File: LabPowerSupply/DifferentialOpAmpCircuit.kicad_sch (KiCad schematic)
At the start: 11 parts

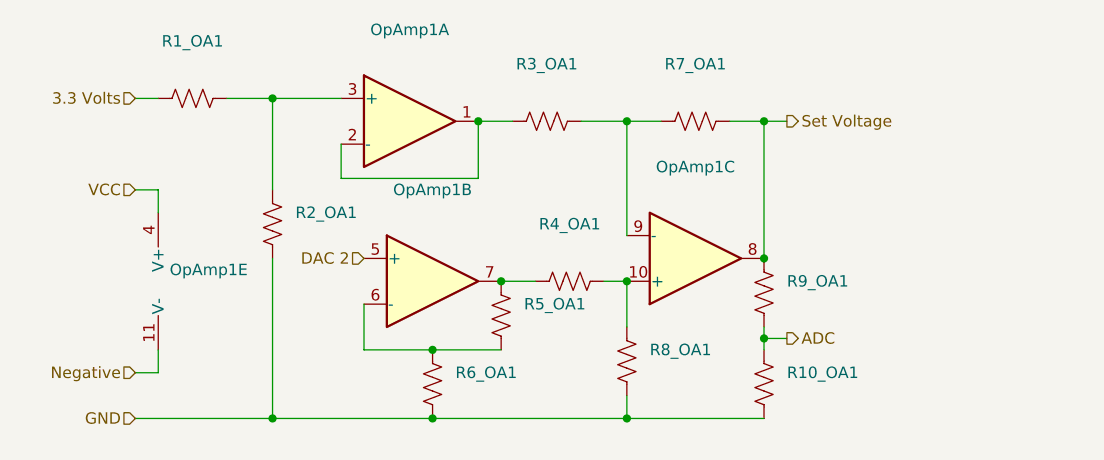
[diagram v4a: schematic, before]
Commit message: Added mcu capacitors, split 5v inductors
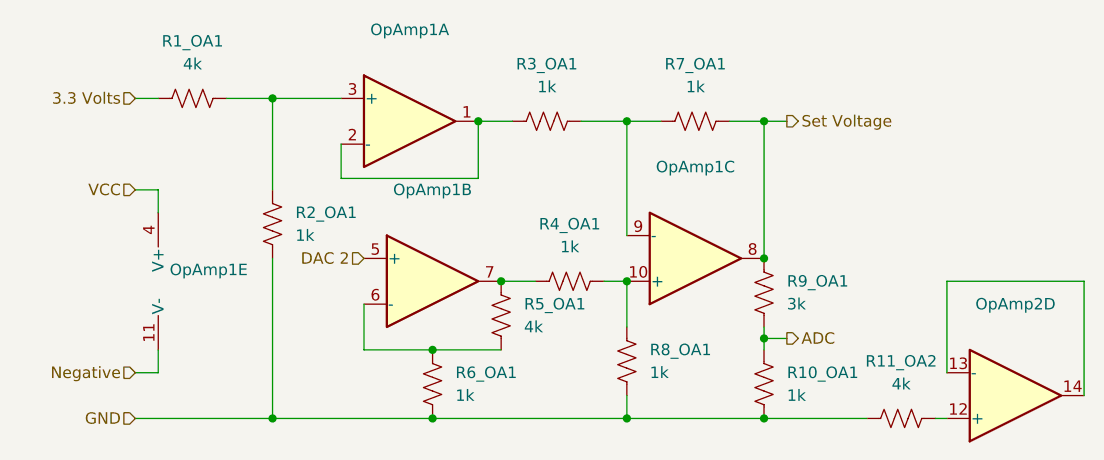
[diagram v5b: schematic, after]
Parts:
- added OpAmp2: (no value), symbol Amplifier_Operational:LM324
- added R11_OA2: 4k, Resistor_SMD:R_0603_1608Metric, symbol Device:R_US
- R10_OA1, R2_OA1, R3_OA1, R4_OA1, R6_OA1, R7_OA1, R8_OA1: value (none) -> 1k; footprint (none) -> Resistor_SMD:R_0603_1608Metric
- R1_OA1, R5_OA1: value (none) -> 4k; footprint (none) -> Resistor_SMD:R_0603_1608Metric
- R9_OA1: value (none) -> 3k; footprint (none) -> Resistor_SMD:R_0603_1608Metric
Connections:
- net GND: now also R11_OA2.1
- new net: OpAmp2.12 (+), R11_OA2.2
- new net: OpAmp2.13 (-), OpAmp2.14
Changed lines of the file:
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@@
   (junction (at 151.13 119.38) (diameter 0) (color 0 0 0 0)
   )
+  (junction (at 166.37 119.38) (diameter 0) (color 0 0 0 0)
+  )
   (junction (at 151.13 86.36) (diameter 0) (color 0 0 0 0)
   )
@@
     (stroke (width 0) (type default) (color 0 0 0 0))
   )
+  (wire (pts (xy 166.37 119.38) (xy 177.8 119.38))
+    (stroke (width 0) (type default) (color 0 0 0 0))
+  )
   (wire (pts (xy 148.59 104.14) (xy 151.13 104.14))
     (stroke (width 0) (type default) (color 0 0 0 0))
   )
+  (wire (pts (xy 201.93 104.14) (xy 186.69 104.14))
+    (stroke (width 0) (type default) (color 0 0 0 0))
+  )
   (wire (pts (xy 166.37 86.36) (xy 168.91 86.36))
     (stroke (width 0) (type default) (color 0 0 0 0))
@@
     (stroke (width 0) (type default) (color 0 0 0 0))
   )
+  (wire (pts (xy 201.93 116.84) (xy 201.93 104.14))
+    (stroke (width 0) (type default) (color 0 0 0 0))
+  )
+  (wire (pts (xy 185.42 119.38) (xy 186.69 119.38))
+    (stroke (width 0) (type default) (color 0 0 0 0))
+  )
   (wire (pts (xy 106.68 83.82) (xy 111.76 83.82))
     (stroke (width 0) (type default) (color 0 0 0 0))
   )
   (wire (pts (xy 140.97 104.14) (xy 137.16 104.14))
+    (stroke (width 0) (type default) (color 0 0 0 0))
+  )
+  (wire (pts (xy 186.69 104.14) (xy 186.69 114.3))
     (stroke (width 0) (type default) (color 0 0 0 0))
   )
@@
       (effects (font (size 1.27 1.27)) (justify left))
     )
-    (property "Value" "" (id 1) (at 168.91 106.6799 0)
-      (effects (font (size 1.27 1.27)) (justify left))
-    )
-    (property "Footprint" "" (id 2) (at 167.386 105.664 90)
+    (property "Value" "3k" (id 1) (at 168.91 106.6799 0)
+      (effects (font (size 1.27 1.27)) (justify left))
+    )
+    (property "Footprint" "Resistor_SMD:R_0603_1608Metric" (id 2) (at 167.386 105.664 90)
       (effects (font (size 1.27 1.27)) hide)
     )
@@
     (in_bom yes) (on_board yes) (fields_autoplaced)
     (property "Reference" "R3_OA1" (id 0) (at 142.24 80.01 90))
-    (property "Value" "" (id 1) (at 142.24 82.55 90))
-    (property "Footprint" "" (id 2) (at 142.494 85.344 90)
+    (property "Value" "1k" (id 1) (at 142.24 82.55 90))
+    (property "Footprint" "Resistor_SMD:R_0603_1608Metric" (id 2) (at 142.494 85.344 90)
       (effects (font (size 1.27 1.27)) hide)
     )
@@
     (in_bom yes) (on_board yes) (fields_autoplaced)
     (property "Reference" "R1_OA1" (id 0) (at 102.87 77.47 90))
-    (property "Value" "" (id 1) (at 102.87 80.01 90))
-    (property "Footprint" "" (id 2) (at 103.124 82.804 90)
+    (property "Value" "4k" (id 1) (at 102.87 80.01 90))
+    (property "Footprint" "Resistor_SMD:R_0603_1608Metric" (id 2) (at 103.124 82.804 90)
       (effects (font (size 1.27 1.27)) hide)
     )
@@
       (effects (font (size 1.27 1.27)) (justify left))
     )
-    (property "Value" "" (id 1) (at 114.3 99.0599 0)
-      (effects (font (size 1.27 1.27)) (justify left))
-    )
-    (property "Footprint" "" (id 2) (at 112.776 98.044 90)
+    (property "Value" "1k" (id 1) (at 114.3 99.0599 0)
+      (effects (font (size 1.27 1.27)) (justify left))
+    )
+    (property "Footprint" "Resistor_SMD:R_0603_1608Metric" (id 2) (at 112.776 98.044 90)
       (effects (font (size 1.27 1.27)) hide)
     )
@@
       (effects (font (size 1.27 1.27)) (justify left))
     )
-    (property "Value" "" (id 1) (at 132.08 116.8399 0)
-      (effects (font (size 1.27 1.27)) (justify left))
-    )
-    (property "Footprint" "" (id 2) (at 130.556 115.824 90)
+    (property "Value" "1k" (id 1) (at 132.08 116.8399 0)
+      (effects (font (size 1.27 1.27)) (justify left))
+    )
+    (property "Footprint" "Resistor_SMD:R_0603_1608Metric" (id 2) (at 130.556 115.824 90)
       (effects (font (size 1.27 1.27)) hide)
     )
@@
     (in_bom yes) (on_board yes) (fields_autoplaced)
     (property "Reference" "R4_OA1" (id 0) (at 144.78 97.79 90))
-    (property "Value" "" (id 1) (at 144.78 100.33 90))
-    (property "Footprint" "" (id 2) (at 145.034 103.124 90)
+    (property "Value" "1k" (id 1) (at 144.78 100.33 90))
+    (property "Footprint" "Resistor_SMD:R_0603_1608Metric" (id 2) (at 145.034 103.124 90)
       (effects (font (size 1.27 1.27)) hide)
     )
     (property "Datasheet" "~" (id 3) (at 144.78 104.14 0)
+      (effects (font (size 1.27 1.27)) hide)
+    )
+    (pin "1")
+    (pin "2")
+  )
+  (symbol (lib_id "Device:R_US") (at 181.61 119.38 90) (unit 1)
+    (in_bom yes) (on_board yes) (fields_autoplaced)
+    (property "Reference" "R11_OA2" (id 0) (at 181.61 113.03 90))
+    (property "Value" "4k" (id 1) (at 181.61 115.57 90))
+    (property "Footprint" "Resistor_SMD:R_0603_1608Metric" (id 2) (at 181.864 118.364 90)
+      (effects (font (size 1.27 1.27)) hide)
+    )
+    (property "Datasheet" "~" (id 3) (at 181.61 119.38 0)
       (effects (font (size 1.27 1.27)) hide)
     )
@@
   )
   (symbol (lib_id "Device:R_US") (at 166.37 115.57 0) (unit 1)
-    (in_bom yes) (on_board yes) (fields_autoplaced)
-    (property "Reference" "R10_OA1" (id 0) (at 168.91 114.2999 0)
-      (effects (font (size 1.27 1.27)) (justify left))
-    )
-    (property "Value" "" (id 1) (at 168.91 116.8399 0)
-      (effects (font (size 1.27 1.27)) (justify left))
-    )
-    (property "Footprint" "" (id 2) (at 167.386 115.824 90)
+    (in_bom yes) (on_board yes)
+    (property "Reference" "R10_OA1" (id 0) (at 168.91 114.3 0)
+      (effects (font (size 1.27 1.27)) (justify left))
+    )
+    (property "Value" "1k" (id 1) (at 168.91 116.8399 0)
+      (effects (font (size 1.27 1.27)) (justify left))
+    )
+    (property "Footprint" "Resistor_SMD:R_0603_1608Metric" (id 2) (at 167.386 115.824 90)
       (effects (font (size 1.27 1.27)) hide)
     )
@@
     (in_bom yes) (on_board yes) (fields_autoplaced)
     (property "Reference" "R7_OA1" (id 0) (at 158.75 80.01 90))
-    (property "Value" "" (id 1) (at 158.75 82.55 90))
-    (property "Footprint" "" (id 2) (at 159.004 85.344 90)
+    (property "Value" "1k" (id 1) (at 158.75 82.55 90))
+    (property "Footprint" "Resistor_SMD:R_0603_1608Metric" (id 2) (at 159.004 85.344 90)
       (effects (font (size 1.27 1.27)) hide)
     )
@@
     (pin "2")
   )
+  (symbol (lib_id "Amplifier_Operational:LM324") (at 194.31 116.84 0) (mirror x) (unit 4)
+    (in_bom yes) (on_board yes) (fields_autoplaced)
+    (property "Reference" "OpAmp2" (id 0) (at 194.31 106.68 0))
+    (property "Value" "" (id 1) (at 194.31 109.22 0))
+    (property "Footprint" "" (id 2) (at 193.04 119.38 0)
+      (effects (font (size 1.27 1.27)) hide)
+    )
+    (property "Datasheet" "http://www.ti.com/lit/ds/symlink/lm2902-n.pdf" (id 3) (at 195.58 121.92 0)
+      (effects (font (size 1.27 1.27)) hide)
+    )
+    (pin "1")
+    (pin "2")
+    (pin "3")
+    (pin "5")
+    (pin "6")
+    (pin "7")
+    (pin "10")
+    (pin "8")
+    (pin "9")
+    (pin "12")
+    (pin "13")
+    (pin "14")
+    (pin "11")
+    (pin "4")
+  )
   (symbol (lib_id "Device:R_US") (at 151.13 113.03 0) (unit 1)
     (in_bom yes) (on_board yes) (fields_autoplaced)
@@
       (effects (font (size 1.27 1.27)) (justify left))
     )
-    (property "Value" "" (id 1) (at 153.67 114.2999 0)
-      (effects (font (size 1.27 1.27)) (justify left))
-    )
-    (property "Footprint" "" (id 2) (at 152.146 113.284 90)
+    (property "Value" "1k" (id 1) (at 153.67 114.2999 0)
+      (effects (font (size 1.27 1.27)) (justify left))
+    )
+    (property "Footprint" "Resistor_SMD:R_0603_1608Metric" (id 2) (at 152.146 113.284 90)
       (effects (font (size 1.27 1.27)) hide)
     )
@@
       (effects (font (size 1.27 1.27)) (justify left))
     )
-    (property "Value" "" (id 1) (at 139.7 109.2199 0)
-      (effects (font (size 1.27 1.27)) (justify left))
-    )
-    (property "Footprint" "" (id 2) (at 138.176 108.204 90)
-      (effects (font (size 1.27 1.27)) hide)
-    )
+    (property "Value" "4k" (id 1) (at 139.7 109.2199 0)
+      (effects (font (size 1.27 1.27)) (justify left))
+    )
+    (property "Footprint" "Resistor_SMD:R_0603_1608Metric" (id 2) (at 138.176 108.204 90)
+      (effects (font (size 1.27 1.27)) hide)
+    )

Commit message: Added oscillator to mcu2
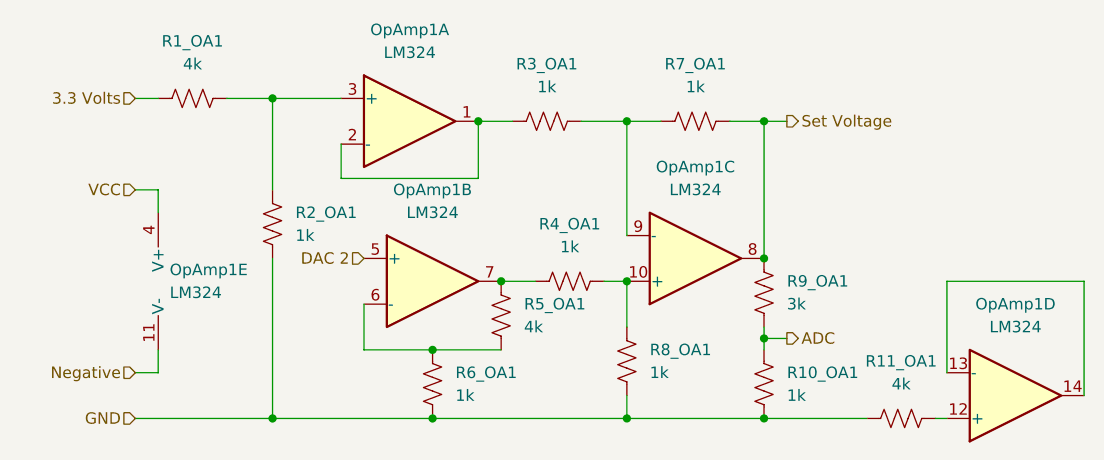
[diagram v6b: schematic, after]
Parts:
- OpAmp1: value (none) -> LM324; footprint (none) -> Package_DIP:DIP-14_W7.62mm
- OpAmp1: renamed from OpAmp2; value (none) -> LM324; footprint (none) -> Package_DIP:DIP-14_W7.62mm
- renumbered R11_OA2 to R11_OA1
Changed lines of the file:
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@@
       (effects (font (size 1.27 1.27)) (justify left))
     )
-    (property "Value" "" (id 1) (at 100.33 105.4099 0)
-      (effects (font (size 1.27 1.27)) (justify left))
-    )
-    (property "Footprint" "" (id 2) (at 100.33 101.6 0)
+    (property "Value" "LM324" (id 1) (at 100.33 105.4099 0)
+      (effects (font (size 1.27 1.27)) (justify left))
+    )
+    (property "Footprint" "Package_DIP:DIP-14_W7.62mm" (id 2) (at 100.33 101.6 0)
       (effects (font (size 1.27 1.27)) hide)
     )
@@
   (symbol (lib_id "Device:R_US") (at 181.61 119.38 90) (unit 1)
     (in_bom yes) (on_board yes) (fields_autoplaced)
-    (property "Reference" "R11_OA2" (id 0) (at 181.61 113.03 90))
+    (property "Reference" "R11_OA1" (id 0) (at 181.61 113.03 90))
     (property "Value" "4k" (id 1) (at 181.61 115.57 90))
     (property "Footprint" "Resistor_SMD:R_0603_1608Metric" (id 2) (at 181.864 118.364 90)
@@
     (in_bom yes) (on_board yes) (fields_autoplaced)
     (property "Reference" "OpAmp1" (id 0) (at 129.54 93.98 0))
-    (property "Value" "" (id 1) (at 129.54 96.52 0))
-    (property "Footprint" "" (id 2) (at 128.27 101.6 0)
+    (property "Value" "LM324" (id 1) (at 129.54 96.52 0))
+    (property "Footprint" "Package_DIP:DIP-14_W7.62mm" (id 2) (at 128.27 101.6 0)
       (effects (font (size 1.27 1.27)) hide)
     )
@@
     (in_bom yes) (on_board yes) (fields_autoplaced)
     (property "Reference" "OpAmp1" (id 0) (at 127 76.2 0))
-    (property "Value" "" (id 1) (at 127 78.74 0))
-    (property "Footprint" "" (id 2) (at 125.73 83.82 0)
+    (property "Value" "LM324" (id 1) (at 127 78.74 0))
+    (property "Footprint" "Package_DIP:DIP-14_W7.62mm" (id 2) (at 125.73 83.82 0)
       (effects (font (size 1.27 1.27)) hide)
     )
@@
   (symbol (lib_id "Amplifier_Operational:LM324") (at 194.31 116.84 0) (mirror x) (unit 4)
     (in_bom yes) (on_board yes) (fields_autoplaced)
-    (property "Reference" "OpAmp2" (id 0) (at 194.31 106.68 0))
-    (property "Value" "" (id 1) (at 194.31 109.22 0))
-    (property "Footprint" "" (id 2) (at 193.04 119.38 0)
+    (property "Reference" "OpAmp1" (id 0) (at 194.31 106.68 0))
+    (property "Value" "LM324" (id 1) (at 194.31 109.22 0))
+    (property "Footprint" "Package_DIP:DIP-14_W7.62mm" (id 2) (at 193.04 119.38 0)
       (effects (font (size 1.27 1.27)) hide)
     )
@@
     (in_bom yes) (on_board yes) (fields_autoplaced)
     (property "Reference" "OpAmp1" (id 0) (at 158.75 91.44 0))
-    (property "Value" "" (id 1) (at 158.75 93.98 0))
-    (property "Footprint" "" (id 2) (at 157.48 104.14 0)
-      (effects (font (size 1.27 1.27)) hide)
-    )
+    (property "Value" "LM324" (id 1) (at 158.75 93.98 0))
+    (property "Footprint" "Package_DIP:DIP-14_W7.62mm" (id 2) (at 157.48 104.14 0)
+      (effects (font (size 1.27 1.27)) hide)
+    )

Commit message: just a commit
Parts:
- R11_OA1: value 4k -> 10k
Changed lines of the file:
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@@
     (in_bom yes) (on_board yes) (fields_autoplaced)
     (property "Reference" "R11_OA1" (id 0) (at 181.61 113.03 90))
-    (property "Value" "4k" (id 1) (at 181.61 115.57 90))
+    (property "Value" "10k" (id 1) (at 181.61 115.57 90))
     (property "Footprint" "Resistor_SMD:R_0603_1608Metric" (id 2) (at 181.864 118.364 90)
       (effects (font (size 1.27 1.27)) hide)

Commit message: Changed most parts to smd
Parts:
- OpAmp1: footprint Package_DIP:DIP-14_W7.62mm -> Package_SO:SOIC-14_3.9x8.7mm_P1.27mm
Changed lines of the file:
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@@
       (effects (font (size 1.27 1.27)) (justify left))
     )
-    (property "Footprint" "Package_DIP:DIP-14_W7.62mm" (id 2) (at 100.33 101.6 0)
+    (property "Footprint" "Package_SO:SOIC-14_3.9x8.7mm_P1.27mm" (id 2) (at 100.33 101.6 0)
       (effects (font (size 1.27 1.27)) hide)
     )
@@
     (property "Reference" "OpAmp1" (id 0) (at 129.54 93.98 0))
     (property "Value" "LM324" (id 1) (at 129.54 96.52 0))
-    (property "Footprint" "Package_DIP:DIP-14_W7.62mm" (id 2) (at 128.27 101.6 0)
+    (property "Footprint" "Package_SO:SOIC-14_3.9x8.7mm_P1.27mm" (id 2) (at 128.27 101.6 0)
       (effects (font (size 1.27 1.27)) hide)
     )
@@
     (property "Reference" "OpAmp1" (id 0) (at 127 76.2 0))
     (property "Value" "LM324" (id 1) (at 127 78.74 0))
-    (property "Footprint" "Package_DIP:DIP-14_W7.62mm" (id 2) (at 125.73 83.82 0)
+    (property "Footprint" "Package_SO:SOIC-14_3.9x8.7mm_P1.27mm" (id 2) (at 125.73 83.82 0)
       (effects (font (size 1.27 1.27)) hide)
     )
@@
     (property "Reference" "OpAmp1" (id 0) (at 194.31 106.68 0))
     (property "Value" "LM324" (id 1) (at 194.31 109.22 0))
-    (property "Footprint" "Package_DIP:DIP-14_W7.62mm" (id 2) (at 193.04 119.38 0)
+    (property "Footprint" "Package_SO:SOIC-14_3.9x8.7mm_P1.27mm" (id 2) (at 193.04 119.38 0)
       (effects (font (size 1.27 1.27)) hide)
     )
@@
     (property "Reference" "OpAmp1" (id 0) (at 158.75 91.44 0))
     (property "Value" "LM324" (id 1) (at 158.75 93.98 0))
-    (property "Footprint" "Package_DIP:DIP-14_W7.62mm" (id 2) (at 157.48 104.14 0)
-      (effects (font (size 1.27 1.27)) hide)
-    )
+    (property "Footprint" "Package_SO:SOIC-14_3.9x8.7mm_P1.27mm" (id 2) (at 157.48 104.14 0)
+      (effects (font (size 1.27 1.27)) hide)
+    )
